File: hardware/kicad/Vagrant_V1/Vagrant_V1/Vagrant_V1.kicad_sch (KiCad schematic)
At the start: 8 parts, among them M1 Motor_DC, M2 Steering_Servo, SW1 SW_DPST_x2

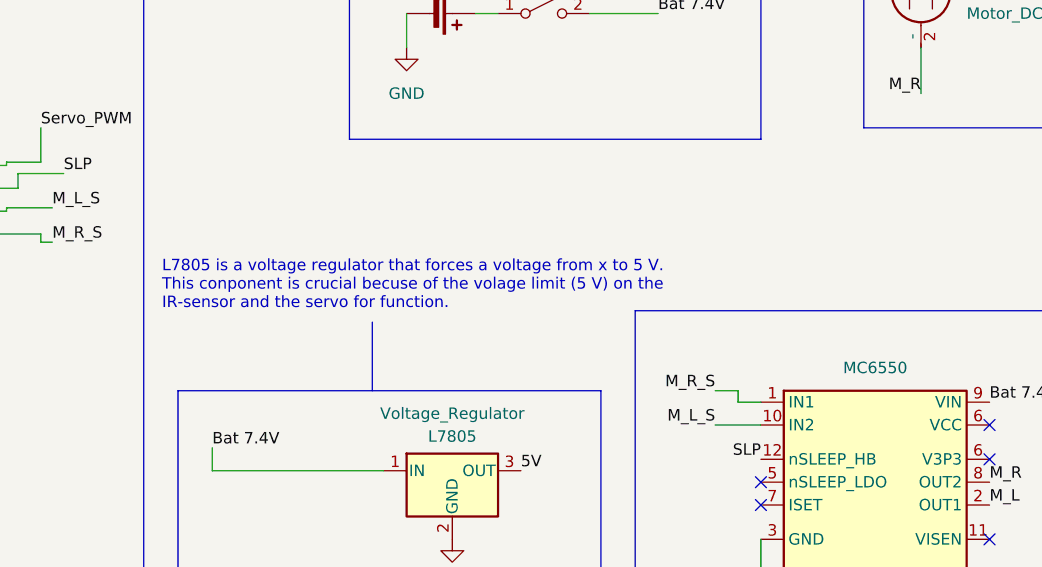
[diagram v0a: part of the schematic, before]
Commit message: Update hardware/kicad/Vagrant_V1/Vagrant_V1/Vagrant_V1.kicad_sch
Co-authored-by: guszahrma <guszahrma@student.gu.se>
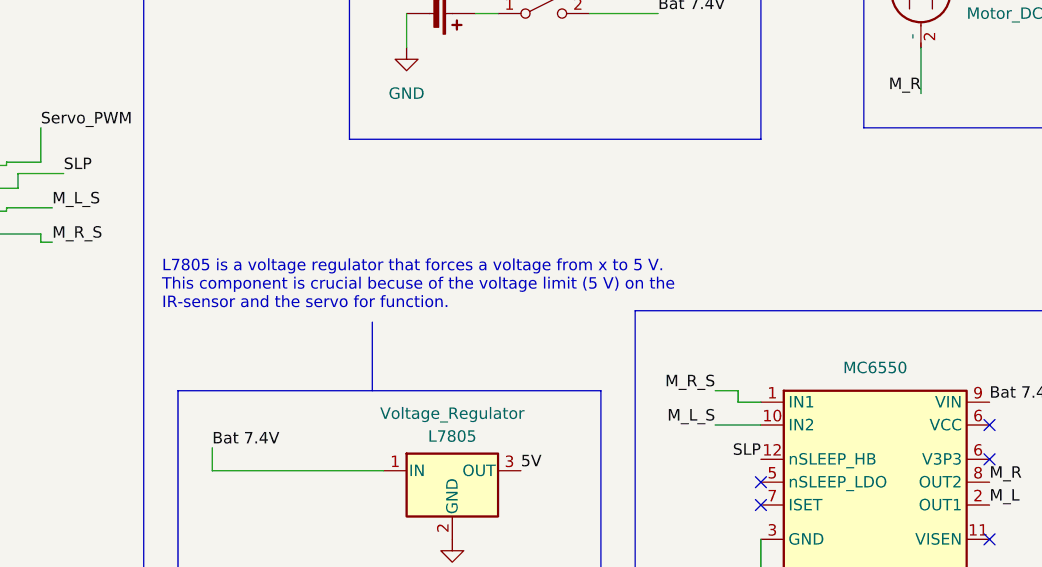
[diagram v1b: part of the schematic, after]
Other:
- note added: "L7805 is a voltage regulator that forces a voltage from x to 5 V. This component is crucial becuse of the voltage limit (5 V) on the IR-sensor and the servo for function."
- note removed: "L7805 is a voltage regulator that forces a voltage from x to 5 V. This conponent is crucial becuse of the volage limit (5 V) on the IR-sensor and the servo for function."
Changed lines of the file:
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@@
 		)
 	)
-	(text "L7805 is a voltage regulator that forces a voltage from x to 5 V. \nThis conponent is crucial becuse of the volage limit (5 V) on the\nIR-sensor and the servo for function. "
+	(text "L7805 is a voltage regulator that forces a voltage from x to 5 V. \nThis component is crucial becuse of the voltage limit (5 V) on the\nIR-sensor and the servo for function. "
 		(exclude_from_sim no)
 		(at 78.232 65.786 0)

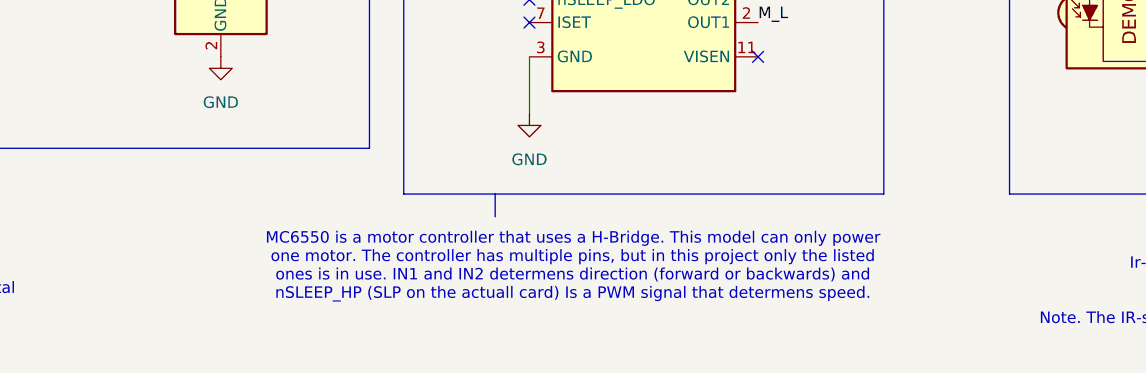
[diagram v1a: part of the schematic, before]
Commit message: Update hardware/kicad/Vagrant_V1/Vagrant_V1/Vagrant_V1.kicad_sch
Co-authored-by: guszahrma <guszahrma@student.gu.se>
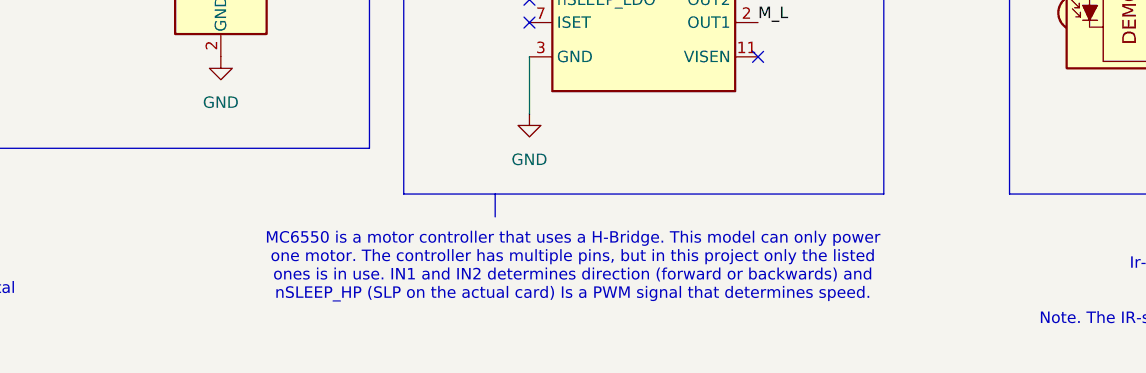
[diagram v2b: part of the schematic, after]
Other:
- note added: "MC6550 is a motor controller that uses a H-Bridge. This model can only power one motor. The controller has multiple pins, but in this project only the listed ones is in use. IN1 and IN2 determines direction (forward or backwards) and nSLEEP_HP (SLP on the actual card) Is a PWM signal that determines speed."
- note removed: "MC6550 is a motor controller that uses a H-Bridge. This model can only power one motor. The controller has multiple pins, but in this project only the listed ones is in use. IN1 and IN2 determens direction (forward or backwards) and nSLEEP_HP (SLP on the actuall card) Is a PWM signal that determens speed."
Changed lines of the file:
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@@
 		)
 	)
-	(text "MC6550 is a motor controller that uses a H-Bridge. This model can only power \none motor. The controller has multiple pins, but in this project only the listed\nones is in use. IN1 and IN2 determens direction (forward or backwards) and \nnSLEEP_HP (SLP on the actuall card) Is a PWM signal that determens speed. "
+	(text "MC6550 is a motor controller that uses a H-Bridge. This model can only power \none motor. The controller has multiple pins, but in this project only the listed\nones is in use. IN1 and IN2 determines direction (forward or backwards) and \nnSLEEP_HP (SLP on the actual card) Is a PWM signal that determines speed. "
 		(exclude_from_sim no)
 		(at 149.606 117.348 0)

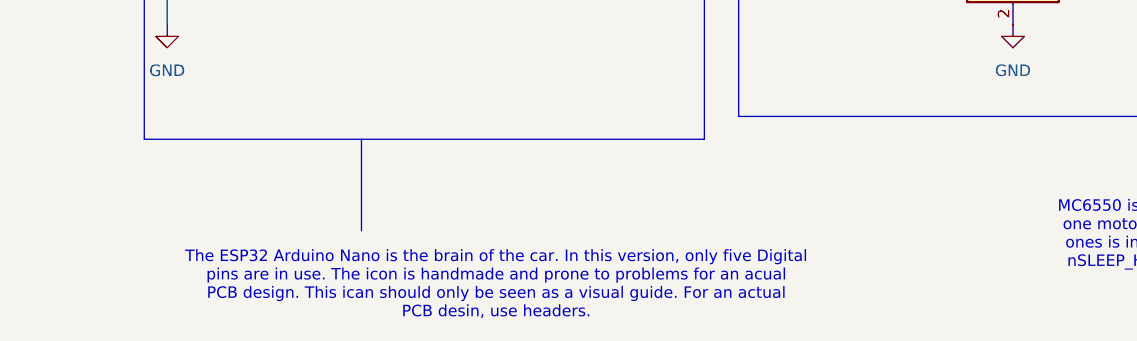
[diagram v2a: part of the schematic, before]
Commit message: Update hardware/kicad/Vagrant_V1/Vagrant_V1/Vagrant_V1.kicad_sch
Co-authored-by: guszahrma <guszahrma@student.gu.se>
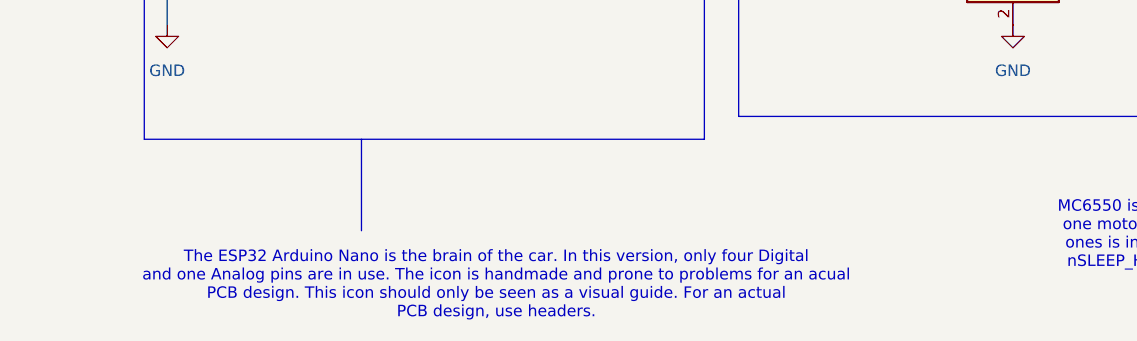
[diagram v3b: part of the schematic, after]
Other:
- note added: "The ESP32 Arduino Nano is the brain of the car. In this version, only four Digital and one Analog pins are in use. The icon is handmade and prone to problems for an acual PCB design. This icon should only be seen as a visual guide. For an actual PCB design, use headers."
- note removed: "The ESP32 Arduino Nano is the brain of the car. In this version, only five Digital pins are in use. The icon is handmade and prone to problems for an acual PCB design. This ican should only be seen as a visual guide. For an actual PCB desin, use headers."
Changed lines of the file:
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@@
 		)
 	)
-	(text "The ESP32 Arduino Nano is the brain of the car. In this version, only five Digital\npins are in use. The icon is handmade and prone to problems for an acual\nPCB design. This ican should only be seen as a visual guide. For an actual\nPCB desin, use headers. "
+	(text "The ESP32 Arduino Nano is the brain of the car. In this version, only four Digital\nand one Analog pins are in use. The icon is handmade and prone to problems for an acual\nPCB design. This icon should only be seen as a visual guide. For an actual\nPCB design, use headers. "
 		(exclude_from_sim no)
 		(at 53.086 122.936 0)

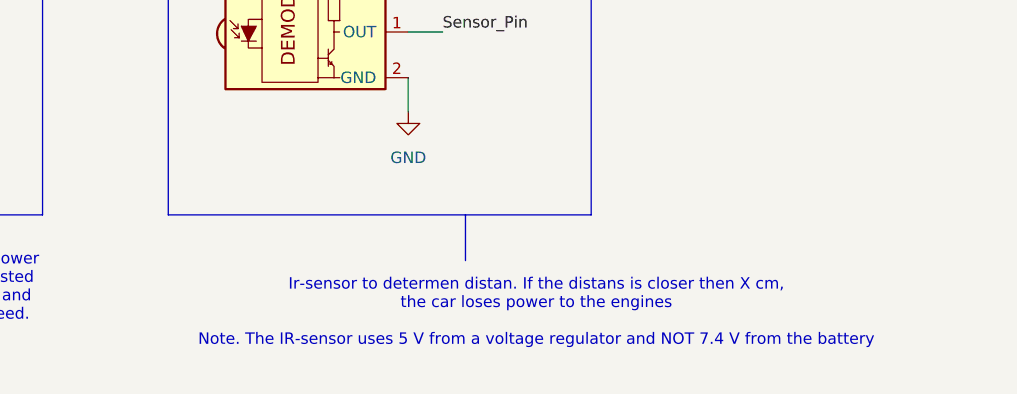
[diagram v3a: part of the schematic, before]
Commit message: Update hardware/kicad/Vagrant_V1/Vagrant_V1/Vagrant_V1.kicad_sch
Co-authored-by: guszahrma <guszahrma@student.gu.se>
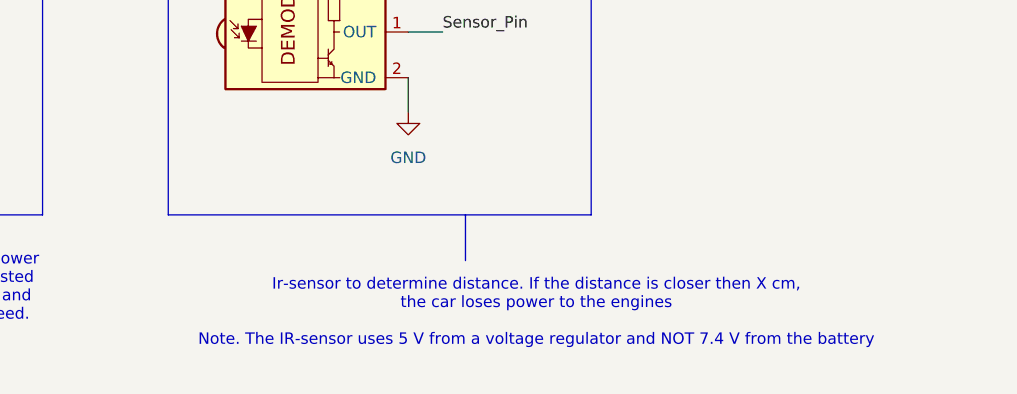
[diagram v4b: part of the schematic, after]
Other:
- note added: "Ir-sensor to determine distance. If the distance is closer then X cm, the car loses power to the engines Note. The IR-sensor uses 5 V from a voltage regulator and NOT 7.4 V from the battery"
- note removed: "Ir-sensor to determen distan. If the distans is closer then X cm, the car loses power to the engines Note. The IR-sensor uses 5 V from a voltage regulator and NOT 7.4 V from the battery"
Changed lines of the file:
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@@
 		)
 	)
-	(text "Ir-sensor to determen distan. If the distans is closer then X cm, \nthe car loses power to the engines\n\nNote. The IR-sensor uses 5 V from a voltage regulator and NOT 7.4 V from the battery"
+	(text "Ir-sensor to determine distance. If the distance is closer then X cm, \nthe car loses power to the engines\n\nNote. The IR-sensor uses 5 V from a voltage regulator and NOT 7.4 V from the battery"
 		(exclude_from_sim no)
 		(at 239.014 120.142 0)
